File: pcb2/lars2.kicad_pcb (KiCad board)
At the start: 2 copper layers, 136 x 114 mm, 32 parts, among them SW1 Encoder, SW2 SW_Push, SW3 SW_Push, SW4 SW_Push, SW5 SW_Push, SW6 SW_Push, SW7 SW_Push, SW8 SW_Push, SW9 SW_Push, U1 Pico, U2 Charger, U3 MOSFET, U4 MOSFET, U5 MOSFET, U6 STEP_UP, U7 STEP_UP, U8 STEP_UP

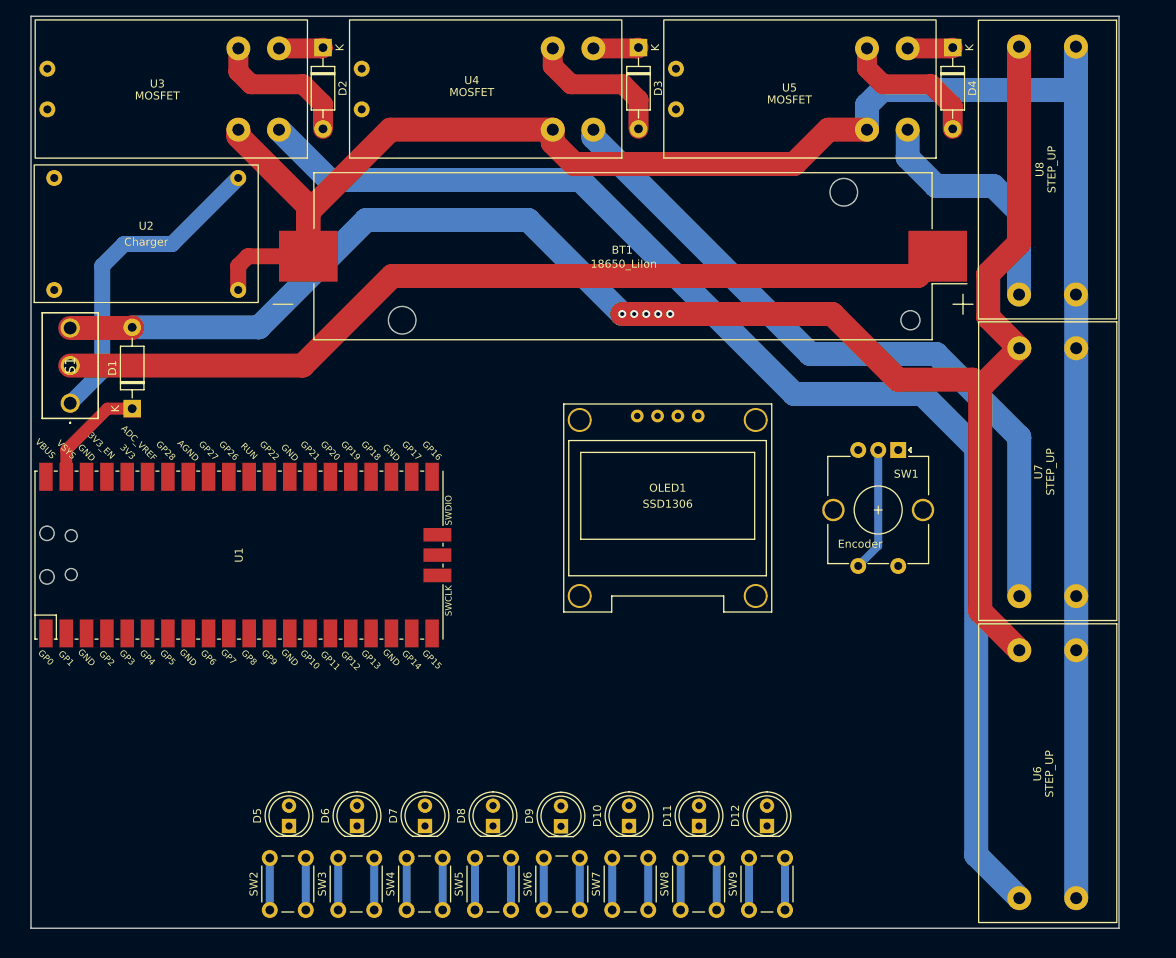
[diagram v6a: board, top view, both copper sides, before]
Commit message: add batt- plane
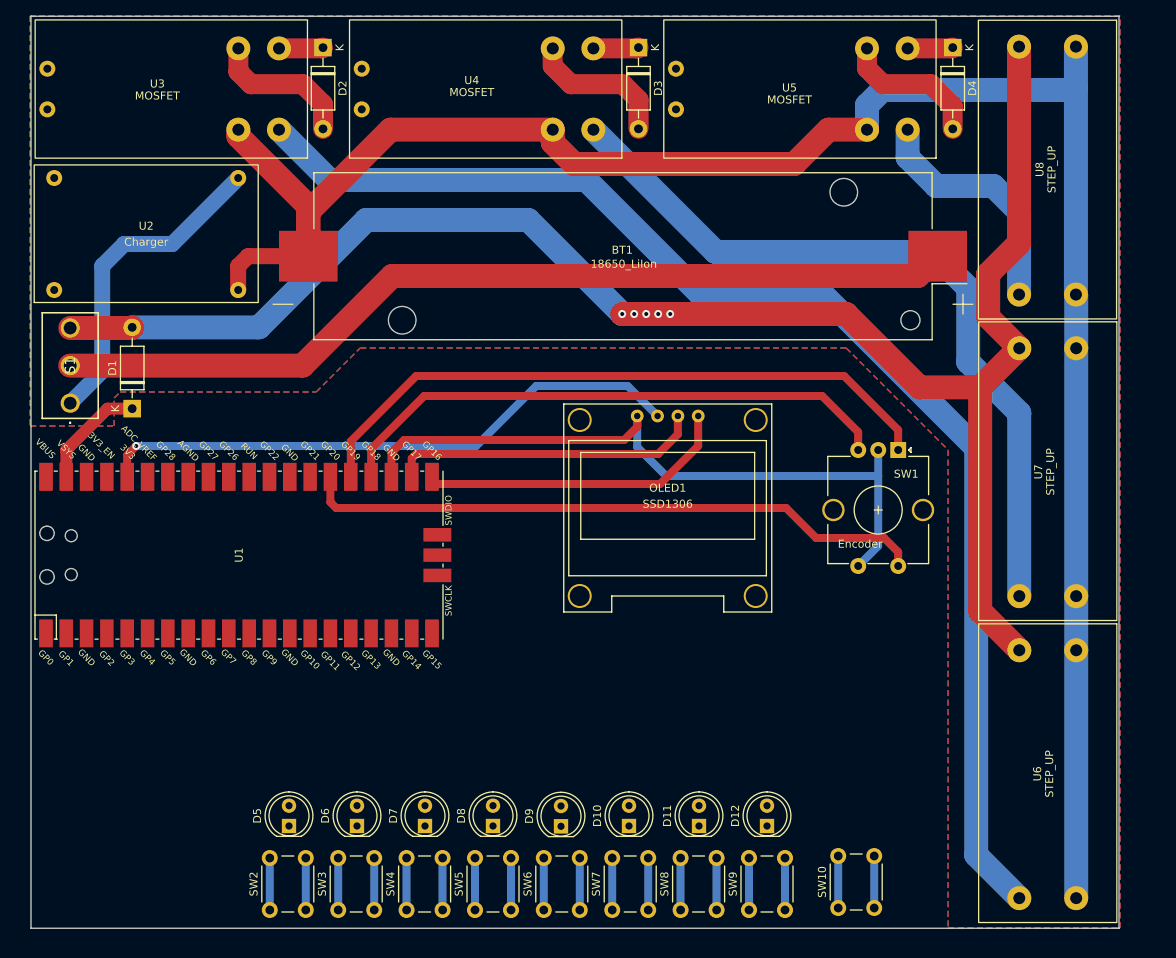
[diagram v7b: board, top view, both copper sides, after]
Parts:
- added SW10: SW_Push, Button_Switch_THT:SW_PUSH_6mm_H5mm, F.Cu at (183.8, 152.2)
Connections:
- OLED1 pad 1: unconnected-(OLED1-GND-Pad1) -> -BATT
- OLED1 pad 2: unconnected-(OLED1-VCC-Pad2) -> +3.3V
- OLED1 pad 3: unconnected-(OLED1-SCL-Pad3) -> Net-(OLED1-SCL)
- OLED1 pad 4: unconnected-(OLED1-SDA-Pad4) -> Net-(OLED1-SDA)
- SW1 pad A: Net-(U1-GPIO17) -> Net-(U1-GPIO19)
- SW1 pad C: GND -> -BATT
- SW1 pad S1: Net-(U1-GPIO16) -> Net-(U1-GPIO20)
- SW1 pad S2: GND -> -BATT
- U1 pad 21: Net-(U1-GPIO16) -> Net-(OLED1-SDA)
- U1 pad 22: Net-(U1-GPIO17) -> Net-(OLED1-SCL)
- U1 pad 23: unconnected-(U1-GND-Pad23) -> -BATT
- U1 pad 25: unconnected-(U1-GPIO19-Pad25) -> Net-(U1-GPIO19)
- U1 pad 26: unconnected-(U1-GPIO20-Pad26) -> Net-(U1-GPIO20)
- U1 pad 27: unconnected-(U1-GPIO21-Pad27) -> Net-(U1-GPIO21)
- U1 pad 29: unconnected-(U1-GPIO22-Pad29) -> Net-(U1-GPIO22)
- U1 pad 31: unconnected-(U1-GPIO26_ADC0-Pad31) -> Net-(U1-GPIO26_ADC0)
- U3 pad 6: unconnected-(U3-trig-Pad6) -> Net-(U1-GPIO26_ADC0)
- U4 pad 6: unconnected-(U4-trig-Pad6) -> Net-(U1-GPIO22)
- U5 pad 6: unconnected-(U5-trig-Pad6) -> Net-(U1-GPIO21)
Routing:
- net -BATT: track 252.4 -> 340.7 mm
- net Net-(U1-GPIO19): track 0.00 -> 82.4 mm
- net Net-(U1-GPIO20): track 0.00 -> 77.6 mm
- net +3.3V: track 0.00 -> 75.0 mm, vias 0 -> 1
- net Net-(U1-GPIO18): track 0.00 -> 72.1 mm
- net Net-(OLED1-SCL): track 0.00 -> 40.0 mm
- net Net-(OLED1-SDA): track 0.00 -> 39.0 mm
- net GND: track 15.5 -> 0.00 mm
- net Net-(U4-Vin+): track 89.6 -> 96.2 mm
- net unconnected-(SW10-Pad2): track 0.00 -> 6.50 mm
- net unconnected-(SW10-Pad1): track 0.00 -> 6.50 mm
- added copper zone on B.Cu, net -BATT
- added copper zone on F.Cu, net -BATT

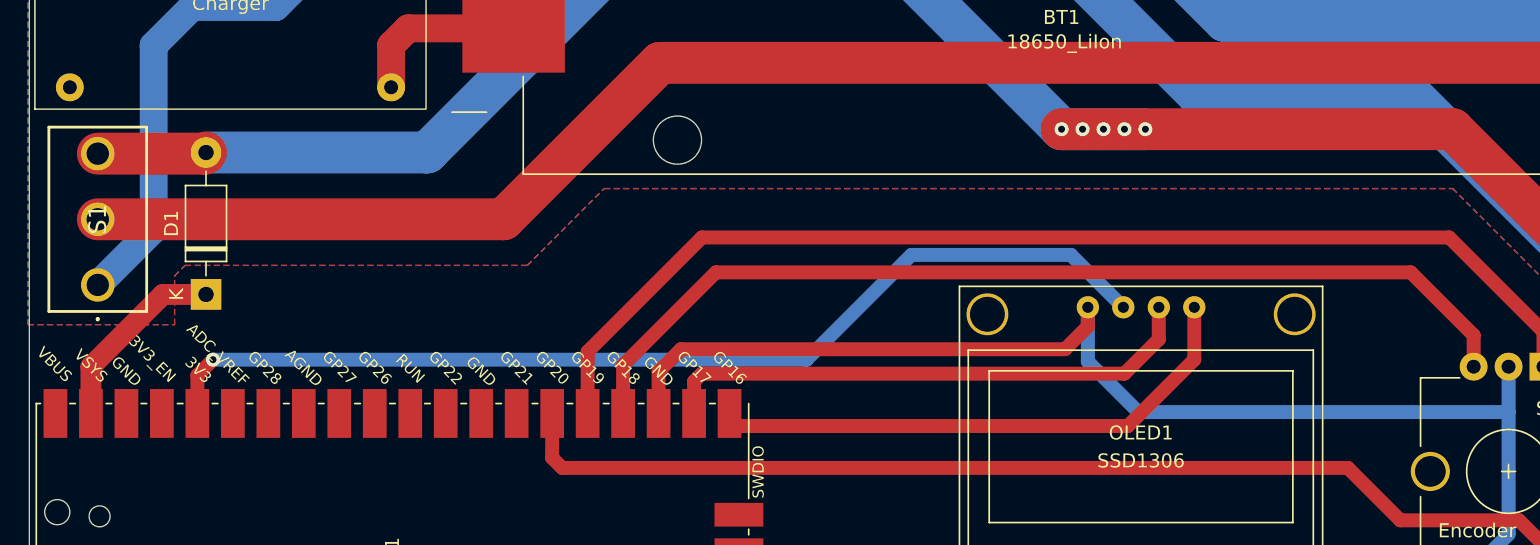
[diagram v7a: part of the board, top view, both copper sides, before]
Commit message: add battery voltage divider to pcb2
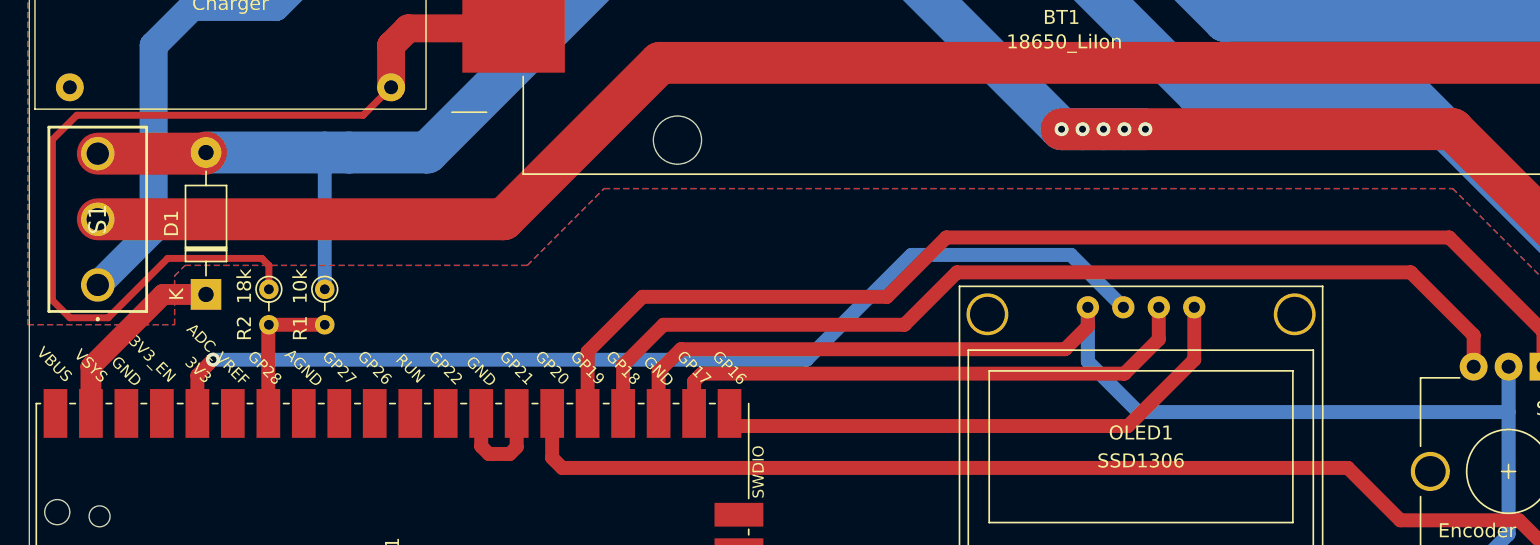
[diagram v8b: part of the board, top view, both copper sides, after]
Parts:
- added R1: 10k, Resistor_THT:R_Axial_DIN0204_L3.6mm_D1.6mm_P2.54mm_Vertical, F.Cu at (104.0, 89.5)
- added R2: 18k, Resistor_THT:R_Axial_DIN0204_L3.6mm_D1.6mm_P2.54mm_Vertical, F.Cu at (100.0, 89.5)
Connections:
- U1 pad 28: unconnected-(U1-GND-Pad28) -> Net-(U1-GPIO21)
- U1 pad 32: unconnected-(U1-GPIO27_ADC1-Pad32) -> Net-(U1-GPIO27_ADC1)
- U1 pad 34: unconnected-(U1-GPIO28_ADC2-Pad34) -> Net-(U1-GPIO28_ADC2)
- U3 pad 6: Net-(U1-GPIO26_ADC0) -> Net-(U1-GPIO27_ADC1)
- U4 pad 6: Net-(U1-GPIO22) -> Net-(U1-GPIO26_ADC0)
- U5 pad 6: Net-(U1-GPIO21) -> Net-(U1-GPIO22)
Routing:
- net -BATT: track 340.7 -> 397.7 mm
- net Net-(U1-GPIO28_ADC2): track 0.00 -> 11.3 mm
- net +BATT: track 216.7 -> 226.5 mm
- net Net-(U1-GPIO21): track 0.00 -> 5.93 mm
